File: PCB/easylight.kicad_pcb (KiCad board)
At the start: 2 copper layers, 40 parts, among them J1 LiPo (1S/3.7V), J2 USB/PWR, J3 LEDs, J4 AVR-ISP, Q1 AO3415_C181094, SW1 SW_1, SW2 SW_2, SW3 SW_3, U1 ATtiny85-20PU, U2 BQ21040DBVR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

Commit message: add TVS for ESD protection, another P-FET for reverse polarity protection
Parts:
- added H3: MountingHole, MountingHole:MountingHole_3.2mm_M3_Pad, F.Cu at (96.5, 19.1)
- added Q2: AO3415_C181094, lcsc:SOT-23-3_L2.9-W1.3-P1.90-LS2.4-BR, F.Cu at (102.6, 17.2)
- D1: value SS34_C8678 -> P6SMB6.8CA-C78395; footprint lcsc:SMA_L4.3-W2.6-LS5.2-RD -> lcsc:SMB_L4.6-W3.6-LS5.3-BI
- moved D1 30.9 mm to (35.6, 16.5)
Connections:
- D1 pad 1: VBUS -> Net-(D1-Pad1)
- F1 pad 1: VBUS -> Net-(D1-Pad1)

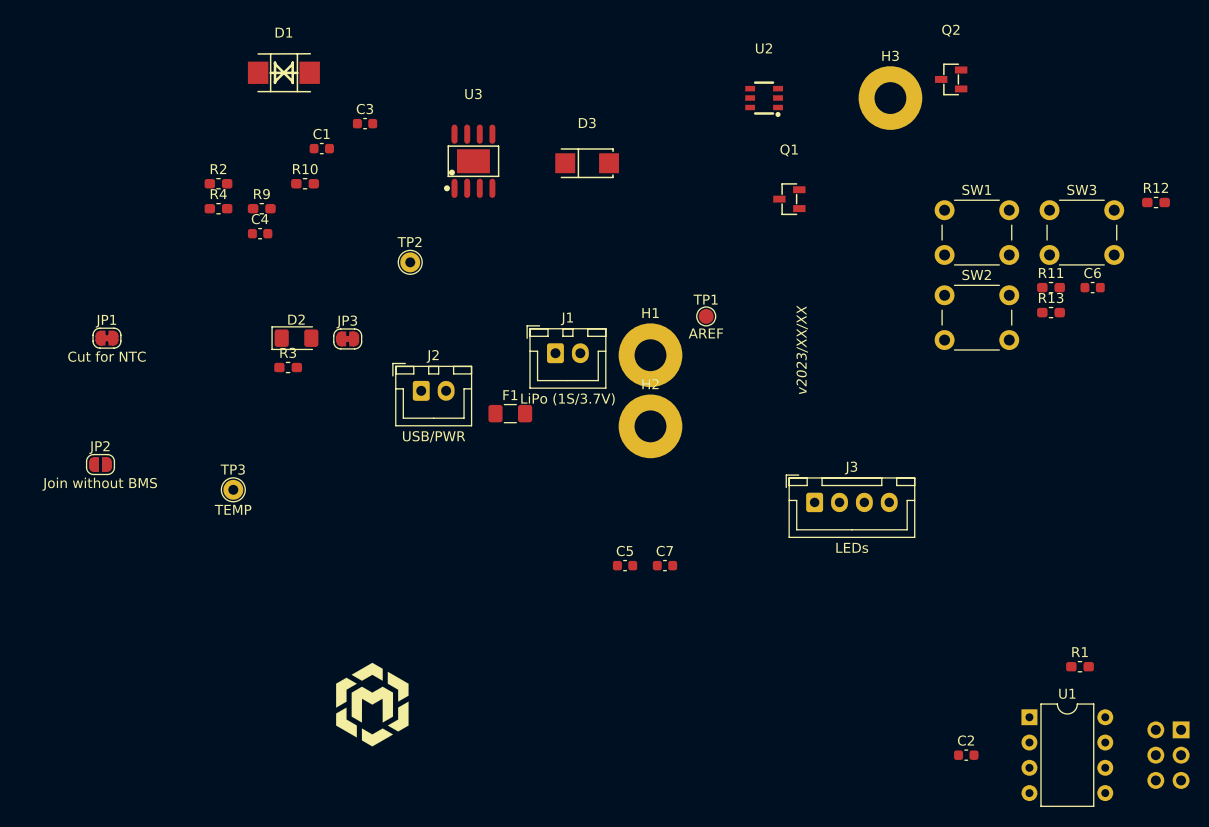
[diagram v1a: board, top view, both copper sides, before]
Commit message: layout PCB, add series resistors for LEDs, remove unused components and add some cosmetics; ratsnest WIP
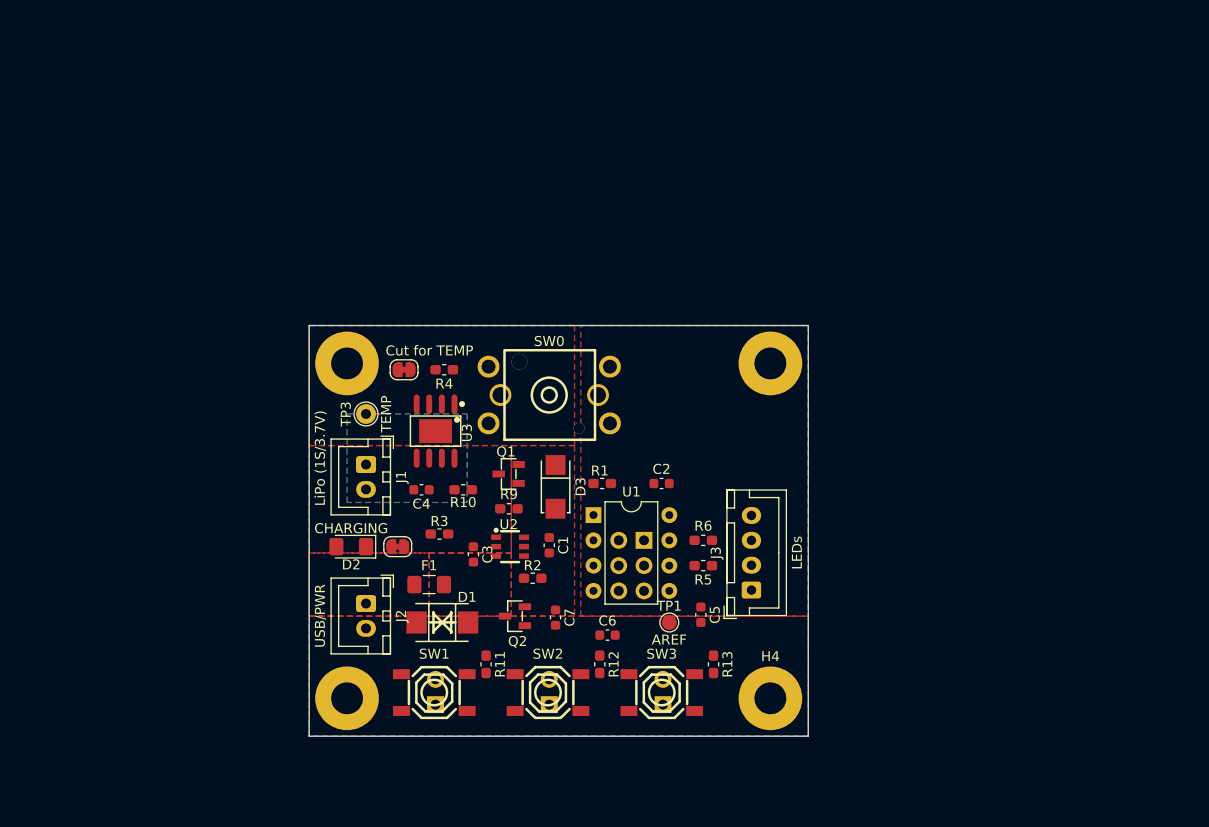
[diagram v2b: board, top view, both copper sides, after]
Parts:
- removed JP3: Cut for LED, Jumper:SolderJumper-2_P1.3mm_Bridged_RoundedPad1.0x1.5mm
- removed TP2: PB4, TestPoint:TestPoint_THTPad_D2.0mm_Drill1.0mm
- added G1: LOGO, Symbol:WEEE-Logo_4.2x6mm_SilkScreen, B.Cu at (56.5, 78.7)
- added H4: MountingHole, MountingHole:MountingHole_3.2mm_M3_Pad, F.Cu at (84.5, 79.4)
- added J5: SW1, Connector_PinHeader_2.54mm:PinHeader_1x02_P2.54mm_Vertical, B.Cu at (50.8, 80.0)
- added J6: SW1, Connector_PinHeader_2.54mm:PinHeader_1x02_P2.54mm_Vertical, B.Cu at (62.2, 80.0)
- added J7: SW1, Connector_PinHeader_2.54mm:PinHeader_1x02_P2.54mm_Vertical, B.Cu at (73.7, 80.0)
- added R5: 220, Resistor_SMD:R_0603_1608Metric_Pad1.05x0.95mm_HandSolder, F.Cu at (77.7, 66.0)
- added R6: 220, Resistor_SMD:R_0603_1608Metric_Pad1.05x0.95mm_HandSolder, F.Cu at (77.7, 63.5)
- added SW0: SPEF110100, lcsc:SW-TH_SPEF110100, F.Cu at (62.2, 48.9)
- added SYM1: SYM_ESD_Small, Symbol:ESD-Logo_6.6x6mm_SilkScreen, B.Cu at (67.9, 78.1)
- D2: value LED -> CHARGING
- JP1: value Cut for NTC -> Cut for TEMP
- JP2: value Join without BMS -> Cut to disable; footprint Jumper:SolderJumper-2_P1.3mm_Open_RoundedPad1.0x1.5mm -> Jumper:SolderJumper-2_P1.3mm_Bridged_RoundedPad1.0x1.5mm
- L1: value MF_Logo -> LOGO; footprint MF custom:mf_logo_10mm -> MF custom:mpc_logo_10mm; moved to B.Cu
- SW1: value SW_1 -> TS-1187A-B-A-B; footprint Button_Switch_THT:SW_PUSH_6mm_H4.3mm -> lcsc:SW-SMD_4P-L5.1-W5.1-P3.70-LS6.5-TL-2
- SW2: value SW_2 -> TS-1187A-B-A-B; footprint Button_Switch_THT:SW_PUSH_6mm_H4.3mm -> lcsc:SW-SMD_4P-L5.1-W5.1-P3.70-LS6.5-TL-2
- SW3: value SW_3 -> TS-1187A-B-A-B; footprint Button_Switch_THT:SW_PUSH_6mm_H4.3mm -> lcsc:SW-SMD_4P-L5.1-W5.1-P3.70-LS6.5-TL-2
- moved R12 72.7 mm to (67.3, 76.0), turned to 270 degrees
- moved SW1 70.6 mm to (50.7, 78.8)
- moved Q2 69.5 mm to (58.8, 71.1)
- moved R11 68.2 mm to (55.9, 76.0), turned to 270 degrees
- moved SW3 62.2 mm to (73.5, 78.8)
- moved C6 60.0 mm to (68.1, 73.0)
- moved D1 57.5 mm to (51.5, 71.8), turned to 180 degrees
- moved J4 57.2 mm to (71.8, 63.5)
- moved SW2 56.4 mm to (62.1, 78.8)
- moved U2 51.8 mm to (58.3, 64.1), turned to 180 degrees
- moved R1 51.4 mm to (67.5, 57.8), turned to 180 degrees
- moved R2 50.7 mm to (60.6, 67.3), turned to 180 degrees
- moved R13 49.0 mm to (78.7, 76.0), turned to 270 degrees
- moved U1 48.3 mm to (66.7, 61.0)
- moved H1 46.0 mm to (41.9, 79.4)
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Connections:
- D2 pad 1: /CHRG -> Net-(D2-Pad1)
- D2 pad 2: Net-(D2-Pad2) -> VBUS
- J1 pad 1: +BATT -> -BATT
- J1 pad 2: -BATT -> +BATT
- J3 pad 2: /D_LEDS -> Net-(J3-Pad2)
- J3 pad 3: /D_LEDS2 -> Net-(J3-Pad3)
- JP2 pad 1: -BATT -> Net-(D2-Pad1)
- JP2 pad 2: GND -> Net-(JP2-Pad2)
- R11 pad 2: Net-(R11-Pad2) -> Net-(J5-Pad2)
- R12 pad 2: Net-(R12-Pad2) -> Net-(J6-Pad2)
- R13 pad 2: Net-(R13-Pad2) -> Net-(J7-Pad2)
- R3 pad 1: Net-(D2-Pad2) -> /CHRG
- R3 pad 2: VCC -> Net-(JP2-Pad2)
- SW1 pad 1: GND -> Net-(J5-Pad2)
- SW1 pad 2: Net-(R11-Pad2) -> Net-(J5-Pad2)
- SW2 pad 1: GND -> Net-(J6-Pad2)
- SW2 pad 2: Net-(R12-Pad2) -> Net-(J6-Pad2)
- SW3 pad 1: GND -> Net-(J7-Pad2)
- SW3 pad 2: Net-(R13-Pad2) -> Net-(J7-Pad2)
- U1 pad 3: Net-(JP3-Pad1) -> /CHRG
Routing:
- added copper zone on F.Cu, net +BATT
- added copper zone on B.Cu, net -BATT
- added copper zone on B.Cu, net GND
- added copper zone on F.Cu, net GND
- added copper zone on F.Cu, net Net-(D1-Pad1)
- added copper zone on F.Cu, net Net-(F1-Pad2)
- added copper zone on F.Cu, net VBUS
- added copper zone on F.Cu, net VCC
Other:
- board outline added: 50.2 x 41.3 mm
- board text added: "Easylight"

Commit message: minor cleanup
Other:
- board text added: "+"
- board text added: "-"
- board text added: "EasyLight"
- board text added: "v2023/01/15"
- board text removed: "Easylight"
- board text removed: "v2023/XX/XX"

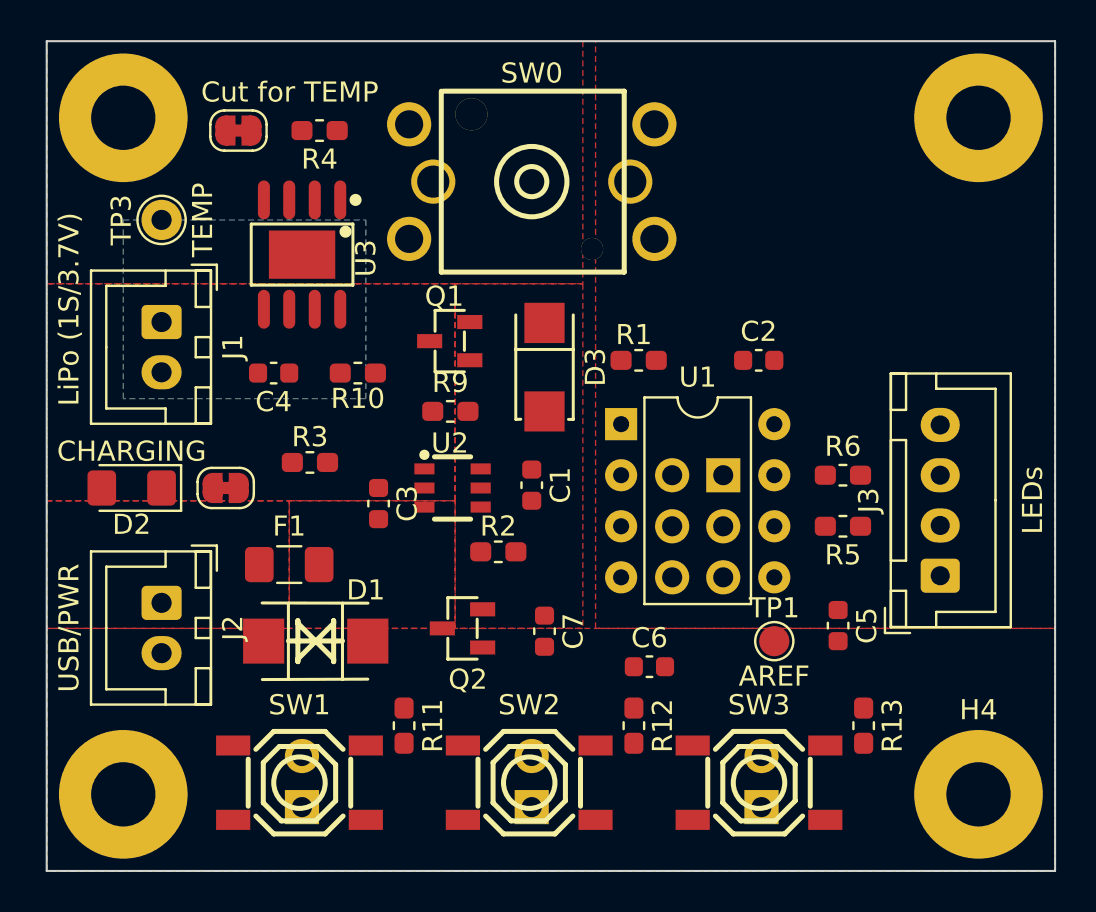
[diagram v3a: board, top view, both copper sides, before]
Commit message: add dedicated pullup for resistor ladder, add docs, finish routing of PCB
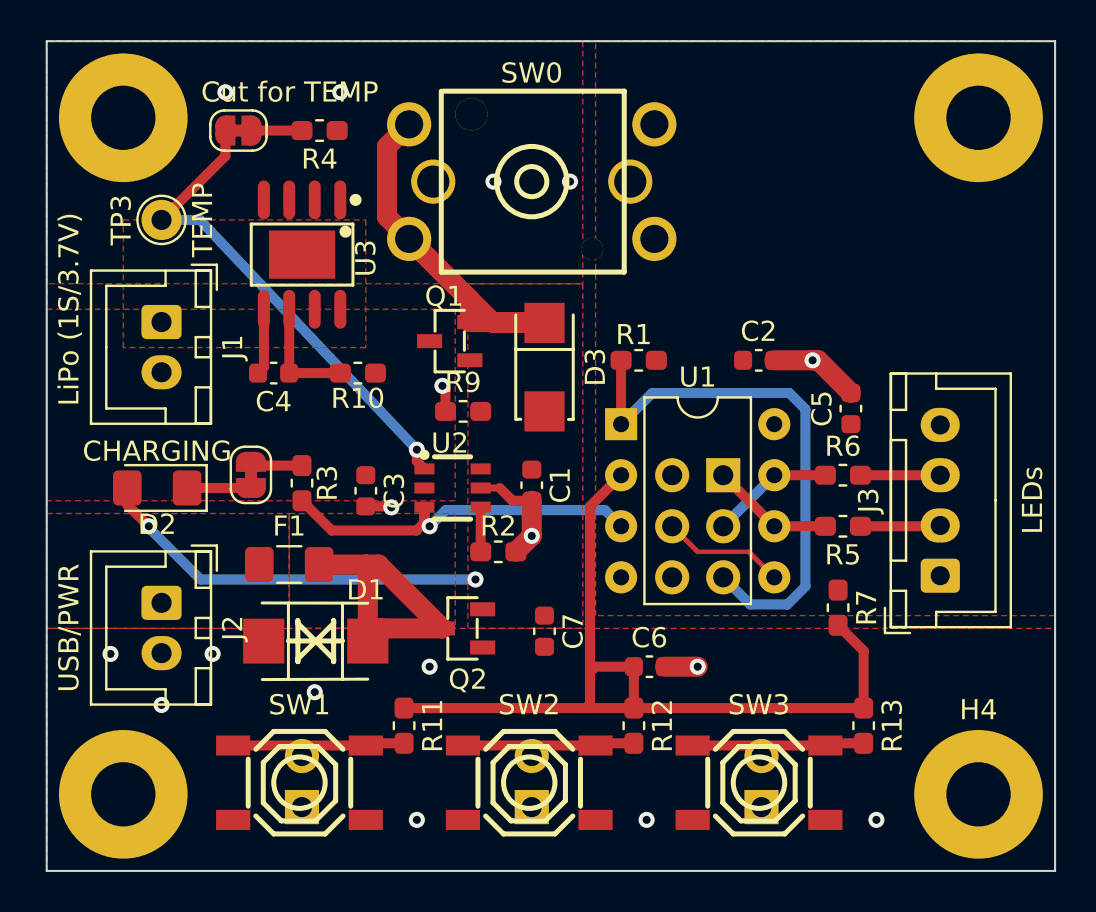
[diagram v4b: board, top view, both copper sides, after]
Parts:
- removed TP1: AREF, TestPoint:TestPoint_Pad_D1.5mm
- added R7: 1k, Resistor_SMD:R_0603_1608Metric_Pad1.05x0.95mm_HandSolder, F.Cu at (77.5, 70.1)
- moved C5 10.8 mm to (78.1, 60.2), turned to 90 degrees
- moved JP2 1.41 mm to (48.3, 63.5), turned to 90 degrees
- moved D2 1.27 mm to (43.6, 64.1)
- moved R3 1.10 mm to (50.8, 63.9), turned to 90 degrees
- moved C3 0.90 mm to (54.0, 64.3)
- moved R9 0.63 mm to (58.8, 60.3)
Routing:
- net /D_switches: track 0.00 -> 44.2 mm
- net /RESET: track 0.00 -> 27.2 mm
- net Net-(JP1-Pad1): track 0.00 -> 25.1 mm, vias 0 -> 1
- net Net-(D3-Pad1): track 0.00 -> 24.2 mm
- net VBUS: track 0.00 -> 19.8 mm, vias 0 -> 2
- net /CHRG: track 0.00 -> 18.9 mm, vias 0 -> 1
- net Net-(D1-Pad1): track 0.00 -> 15.3 mm
- net GND: track 0.00 -> 14.4 mm, vias 0 -> 17
- net Net-(J6-Pad2): track 0.00 -> 9.12 mm
- net Net-(J5-Pad2): track 0.00 -> 9.12 mm
- net Net-(J7-Pad2): track 0.00 -> 9.12 mm
- net /D_LEDS2: track 0.00 -> 6.13 mm
- net /D_LEDS: track 0.00 -> 6.13 mm
- net /AREF: track 0.00 -> 6.13 mm
- net Net-(C4-Pad1): track 0.00 -> 5.72 mm
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- added copper zone on F.Cu, net -BATT
- removed copper zone on B.Cu, net -BATT
